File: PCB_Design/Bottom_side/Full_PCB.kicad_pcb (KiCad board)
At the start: 4 copper layers, 94 x 94 mm, 165 parts, among them Q1 Q_NMOS_GSD, Q10 Q_PMOS_GSD, Q11 Q_PMOS_GSD, Q12 Q_PMOS_GSD, Q2 Q_NMOS_GSD, Q3 Q_NMOS_GSD, Q4 Q_NMOS_GSD, Q5 Q_PMOS_GSD, Q6 Q_PMOS_GSD, Q7 Q_PMOS_GSD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

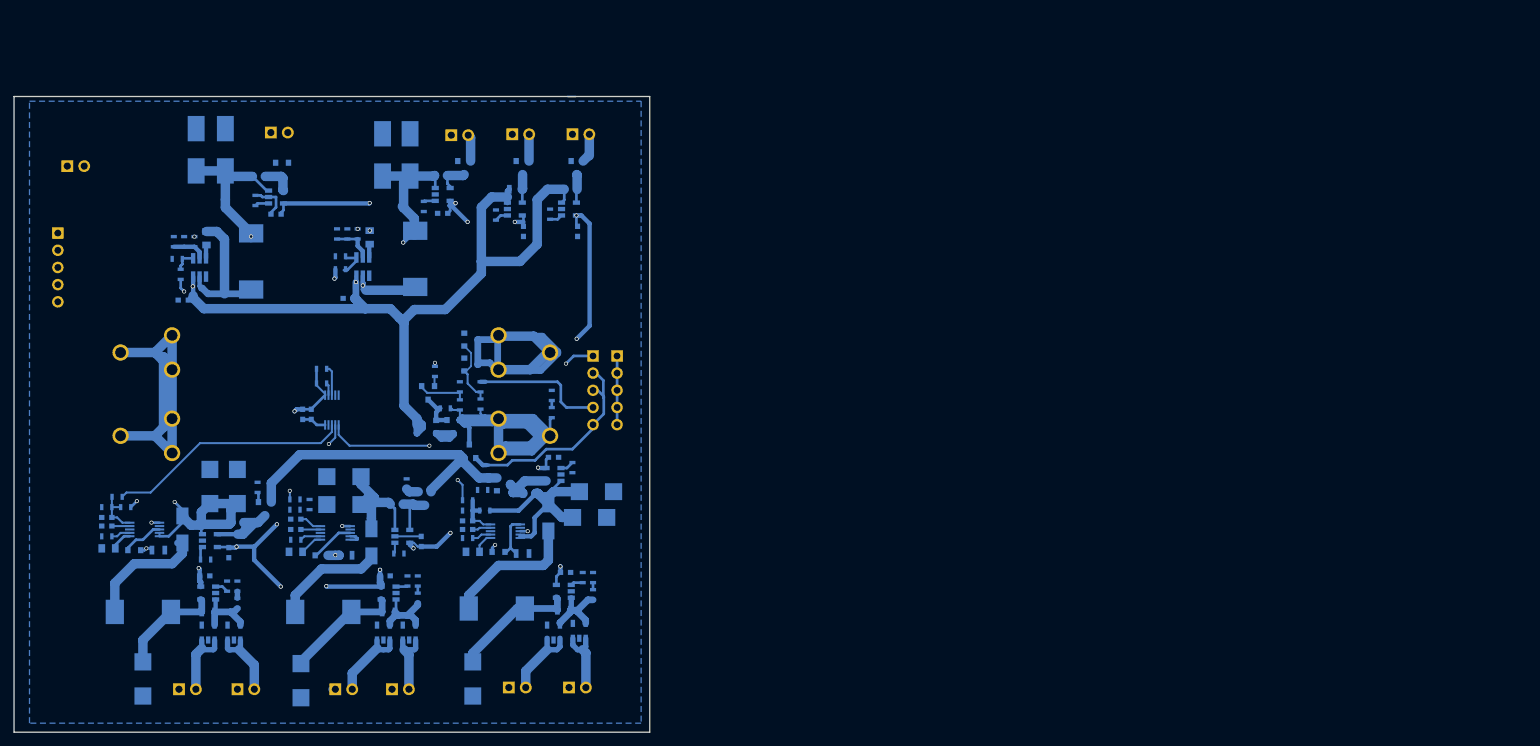
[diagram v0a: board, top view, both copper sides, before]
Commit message: Updated PCB structure tree
Full_PCB now includes bottom and top layer hierarchical sheets
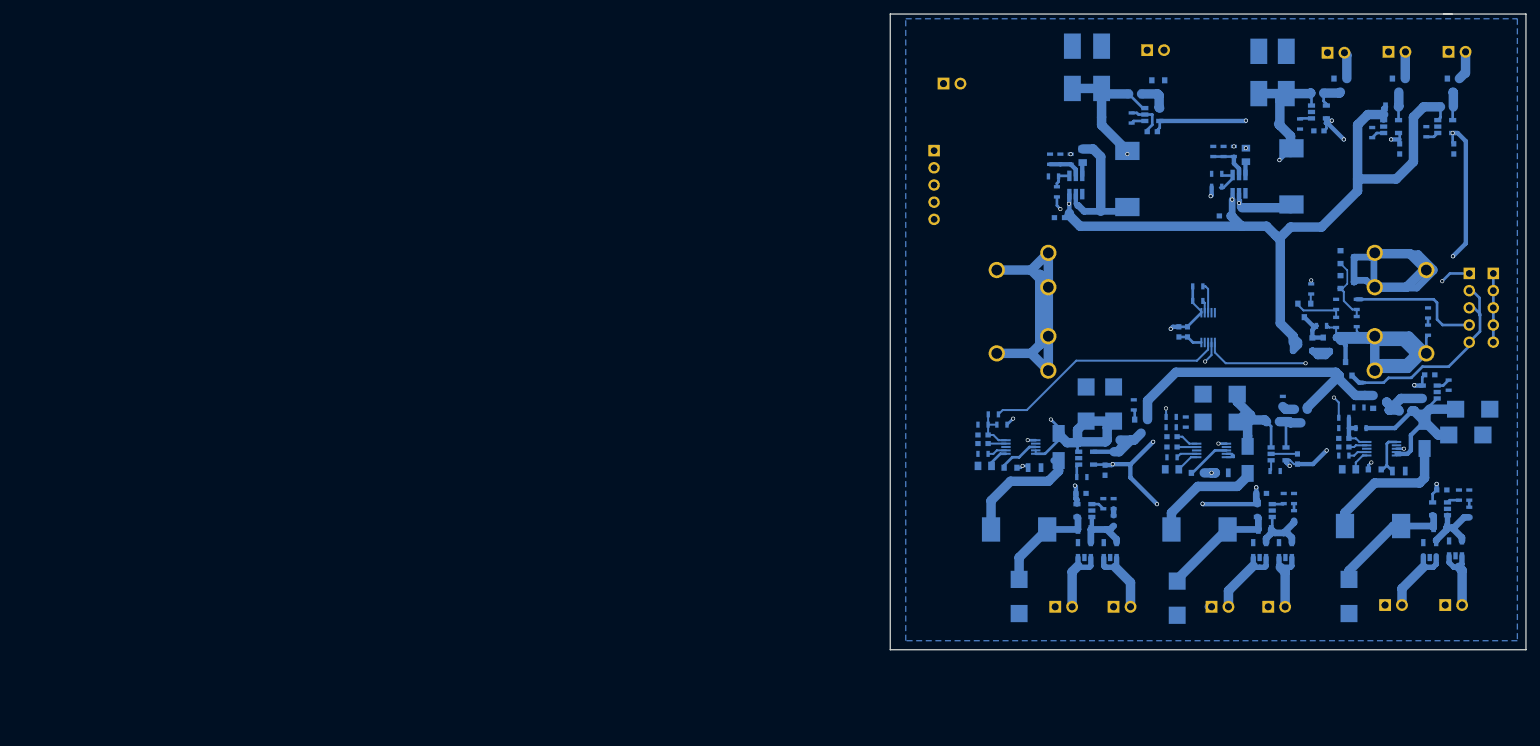
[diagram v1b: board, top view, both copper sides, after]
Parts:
- moved 20m2 130.1 mm to (238.2, 85.0)
- moved 20m7 130.1 mm to (244.7, 36.4)
- moved 20m8 130.1 mm to (217.8, 36.5)
- moved 5V_ind1 130.1 mm to (240.9, 48.7)
- moved 5V_ind2 130.1 mm to (216.7, 49.1)
- moved BT1 130.1 mm to (253.2, 74.9)
- moved BT2 130.1 mm to (205.0, 62.5)
- moved Batt_V_1 130.1 mm to (255.3, 30.3)
- moved Batt_V_2 130.1 mm to (264.2, 30.3)
- moved C1 130.1 mm to (210.6, 82.4)
- moved C5 130.1 mm to (267.7, 83.1)
- moved CBulk2 130.1 mm to (240.2, 33.3)
- moved CBulk4 130.1 mm to (212.9, 32.6)
- moved CMAX1 130.1 mm to (195.6, 91.5)
- moved CVCCbuck1 130.1 mm to (231.0, 54.5)
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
